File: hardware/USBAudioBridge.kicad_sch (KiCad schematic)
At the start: 2 parts

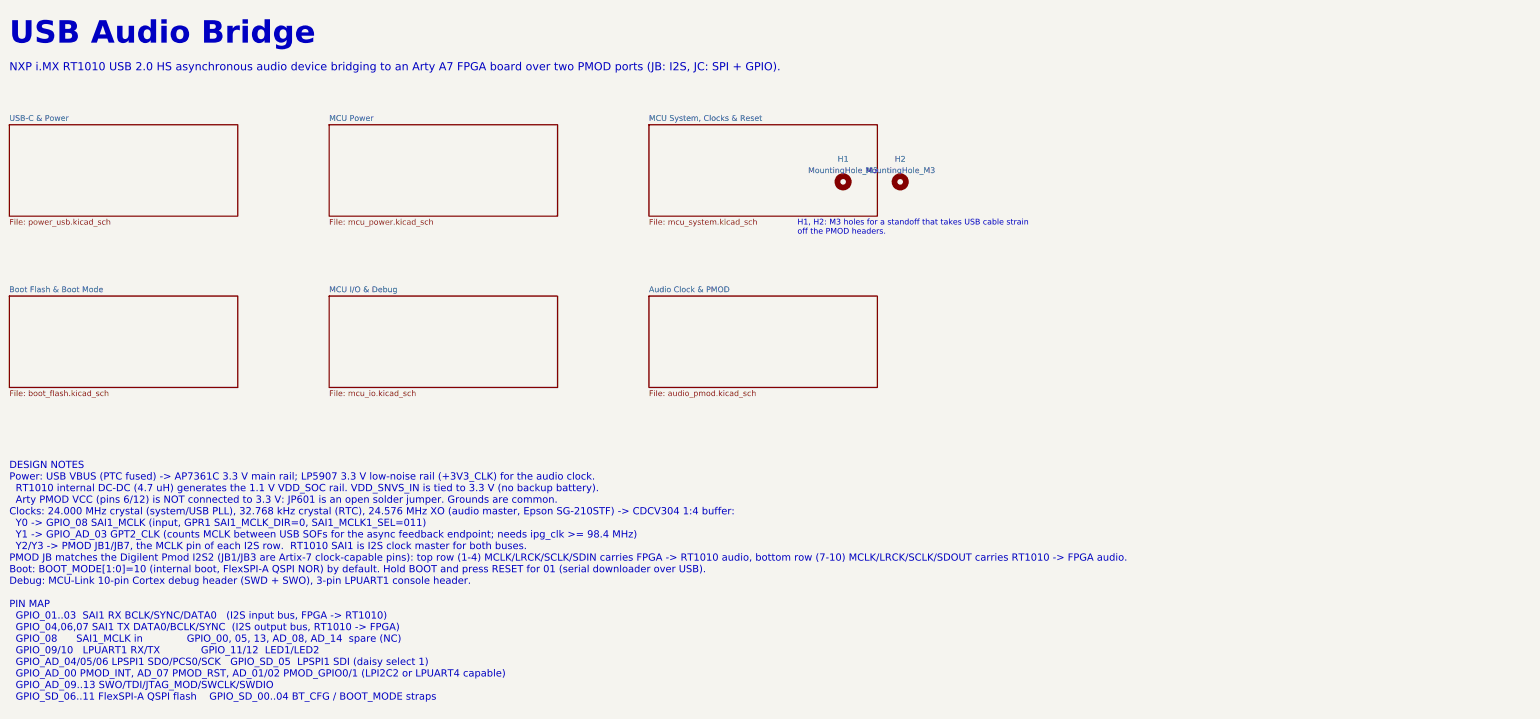
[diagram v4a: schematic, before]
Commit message: Add fab pipeline, sourcing, CI and developer reference manual
- tools/fab.py: ERC/DRC gate, then JLCPCB (LCSC BOM, rotation-corrected
  CPL) and PCBWay (MPN BOM, centroid) packages with Gerbers, drill,
  assembly drawings, schematic PDF and order notes
- .github/workflows/fab.yml: runs fab.py in kicad/kicad:10.0.7; artifacts
  on push/PR, release assets on v* tags
- design.py: MPN/Manufacturer/LCSC for every BOM line (checked against
  JLCPCB stock); SG-210SCBA oscillator, Liming 200 uW 24 MHz crystal,
  PTS810SJG switches, USB4105-GF-A-120, ~2 V LEDs
- R603 DNP: GPT2 cannot count 24.576 MHz (external clock < PERCLK/4,
  PERCLK <= 75 MHz); async feedback comes from SAI sample counts
- Via drill 0.3 -> 0.2 mm (pads unchanged) for PCBWay's 5 mil ring
- Drill/place origin at the board's lower-left corner; legible Fab refs
- pcb.py --sync-fields updates fields/DNP without re-routing
- docs/reference-manual.md: RT1010 firmware and Arty A7 reference
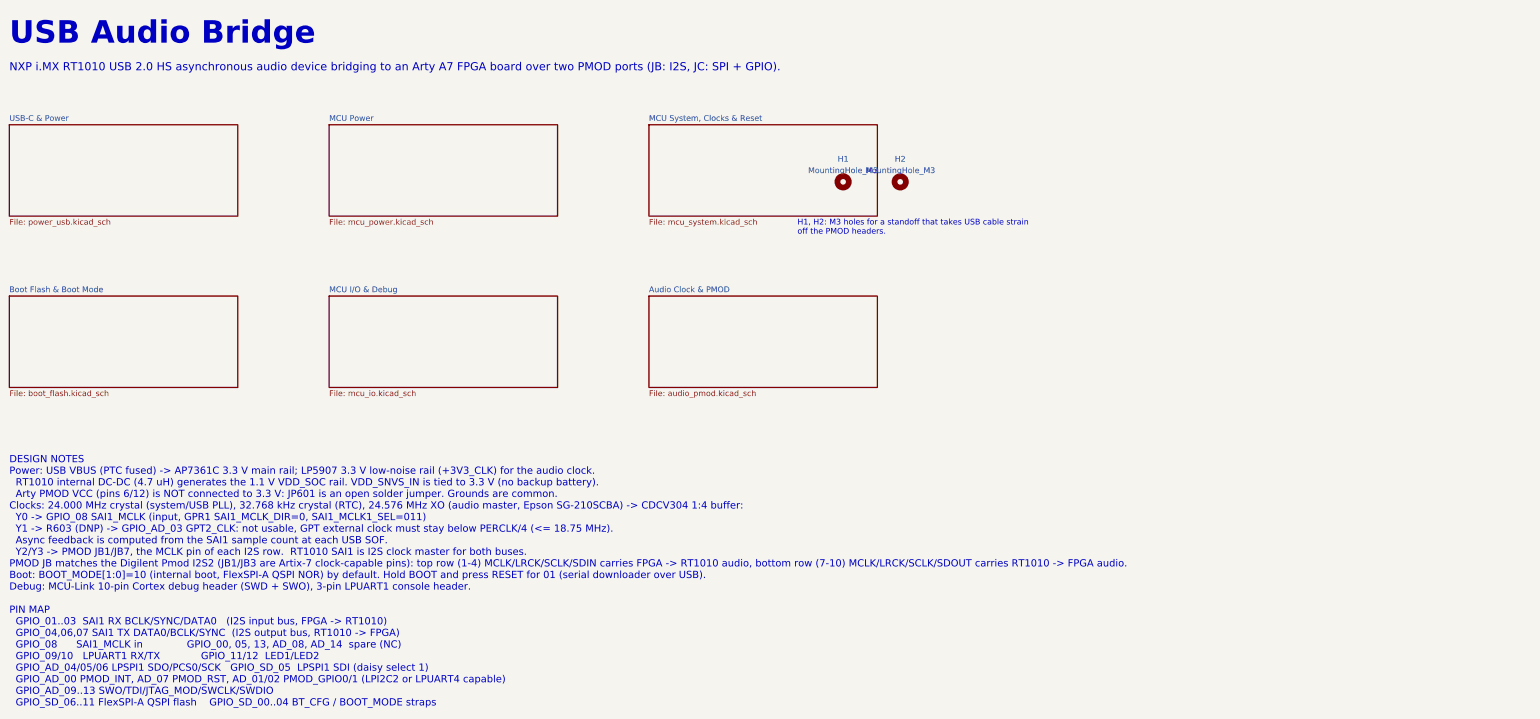
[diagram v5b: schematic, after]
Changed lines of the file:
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@@
 		)
 	)
-	(text "DESIGN NOTES\nPower: USB VBUS (PTC fused) -> AP7361C 3.3 V main rail; LP5907 3.3 V low-noise rail (+3V3_CLK) for the audio clock.\n  RT1010 internal DC-DC (4.7 uH) generates the 1.1 V VDD_SOC rail. VDD_SNVS_IN is tied to 3.3 V (no backup battery).\n  Arty PMOD VCC (pins 6/12) is NOT connected to 3.3 V: JP601 is an open solder jumper. Grounds are common.\nClocks: 24.000 MHz crystal (system/USB PLL), 32.768 kHz crystal (RTC), 24.576 MHz XO (audio master, Epson SG-210STF) -> CDCV304 1:4 buffer:\n  Y0 -> GPIO_08 SAI1_MCLK (input, GPR1 SAI1_MCLK_DIR=0, SAI1_MCLK1_SEL=011)\n  Y1 -> GPIO_AD_03 GPT2_CLK (counts MCLK between USB SOFs for the async feedback endpoint; needs ipg_clk >= 98.4 MHz)\n  Y2/Y3 -> PMOD JB1/JB7, the MCLK pin of each I2S row.  RT1010 SAI1 is I2S clock master for both buses.\nPMOD JB matches the Digilent Pmod I2S2 (JB1/JB3 are Artix-7 clock-capable pins): top row (1-4) MCLK/LRCK/SCLK/SDIN carries FPGA -> RT1010 audio, bottom row (7-10) MCLK/LRCK/SCLK/SDOUT carries RT1010 -> FPGA audio.\nBoot: BOOT_MODE[1:0]=10 (internal boot, FlexSPI-A QSPI NOR) by default. Hold BOOT and press RESET for 01 (serial downloader over USB).\nDebug: MCU-Link 10-pin Cortex debug header (SWD + SWO), 3-pin LPUART1 console header.\n\nPIN MAP\n  GPIO_01..03  SAI1 RX BCLK/SYNC/DATA0   (I2S input bus, FPGA -> RT1010)\n  GPIO_04,06,07 SAI1 TX DATA0/BCLK/SYNC  (I2S output bus, RT1010 -> FPGA)\n  GPIO_08      SAI1_MCLK in              GPIO_00, 05, 13, AD_08, AD_14  spare (NC)\n  GPIO_09/10   LPUART1 RX/TX             GPIO_11/12  LED1/LED2\n  GPIO_AD_04/05/06 LPSPI1 SDO/PCS0/SCK   GPIO_SD_05  LPSPI1 SDI (daisy select 1)\n  GPIO_AD_00 PMOD_INT, AD_07 PMOD_RST, AD_01/02 PMOD_GPIO0/1 (LPI2C2 or LPUART4 capable)\n  GPIO_AD_09..13 SWO/TDI/JTAG_MOD/SWCLK/SWDIO\n  GPIO_SD_06..11 FlexSPI-A QSPI flash    GPIO_SD_00..04 BT_CFG / BOOT_MODE straps"
+	(text "DESIGN NOTES\nPower: USB VBUS (PTC fused) -> AP7361C 3.3 V main rail; LP5907 3.3 V low-noise rail (+3V3_CLK) for the audio clock.\n  RT1010 internal DC-DC (4.7 uH) generates the 1.1 V VDD_SOC rail. VDD_SNVS_IN is tied to 3.3 V (no backup battery).\n  Arty PMOD VCC (pins 6/12) is NOT connected to 3.3 V: JP601 is an open solder jumper. Grounds are common.\nClocks: 24.000 MHz crystal (system/USB PLL), 32.768 kHz crystal (RTC), 24.576 MHz XO (audio master, Epson SG-210SCBA) -> CDCV304 1:4 buffer:\n  Y0 -> GPIO_08 SAI1_MCLK (input, GPR1 SAI1_MCLK_DIR=0, SAI1_MCLK1_SEL=011)\n  Y1 -> R603 (DNP) -> GPIO_AD_03 GPT2_CLK: not usable, GPT external clock must stay below PERCLK/4 (<= 18.75 MHz).\n  Async feedback is computed from the SAI1 sample count at each USB SOF.\n  Y2/Y3 -> PMOD JB1/JB7, the MCLK pin of each I2S row.  RT1010 SAI1 is I2S clock master for both buses.\nPMOD JB matches the Digilent Pmod I2S2 (JB1/JB3 are Artix-7 clock-capable pins): top row (1-4) MCLK/LRCK/SCLK/SDIN carries FPGA -> RT1010 audio, bottom row (7-10) MCLK/LRCK/SCLK/SDOUT carries RT1010 -> FPGA audio.\nBoot: BOOT_MODE[1:0]=10 (internal boot, FlexSPI-A QSPI NOR) by default. Hold BOOT and press RESET for 01 (serial downloader over USB).\nDebug: MCU-Link 10-pin Cortex debug header (SWD + SWO), 3-pin LPUART1 console header.\n\nPIN MAP\n  GPIO_01..03  SAI1 RX BCLK/SYNC/DATA0   (I2S input bus, FPGA -> RT1010)\n  GPIO_04,06,07 SAI1 TX DATA0/BCLK/SYNC  (I2S output bus, RT1010 -> FPGA)\n  GPIO_08      SAI1_MCLK in              GPIO_00, 05, 13, AD_08, AD_14  spare (NC)\n  GPIO_09/10   LPUART1 RX/TX             GPIO_11/12  LED1/LED2\n  GPIO_AD_04/05/06 LPSPI1 SDO/PCS0/SCK   GPIO_SD_05  LPSPI1 SDI (daisy select 1)\n  GPIO_AD_00 PMOD_INT, AD_07 PMOD_RST, AD_01/02 PMOD_GPIO0/1 (LPI2C2 or LPUART4 capable)\n  GPIO_AD_09..13 SWO/TDI/JTAG_MOD/SWCLK/SWDIO\n  GPIO_SD_06..11 FlexSPI-A QSPI flash    GPIO_SD_00..04 BT_CFG / BOOT_MODE straps"
 		(exclude_from_sim no)
 		(at 30.48 152.4 0)
